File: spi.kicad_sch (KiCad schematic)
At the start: 24 parts

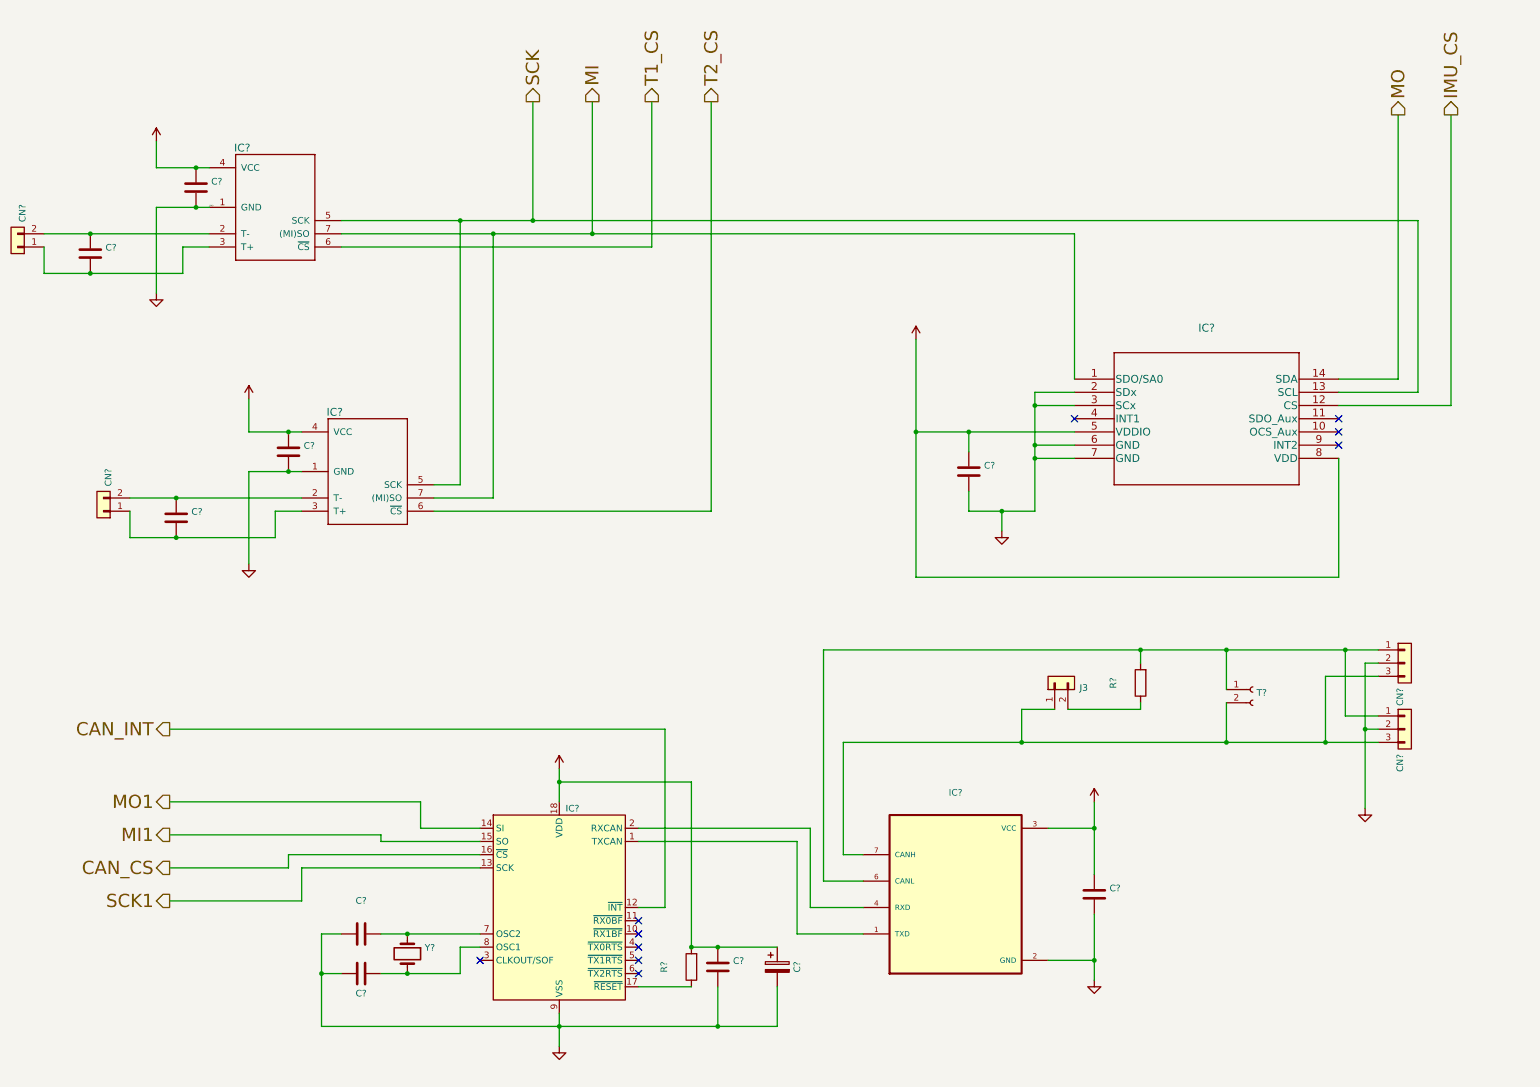
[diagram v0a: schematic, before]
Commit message: fixed power flag in schematic causing error
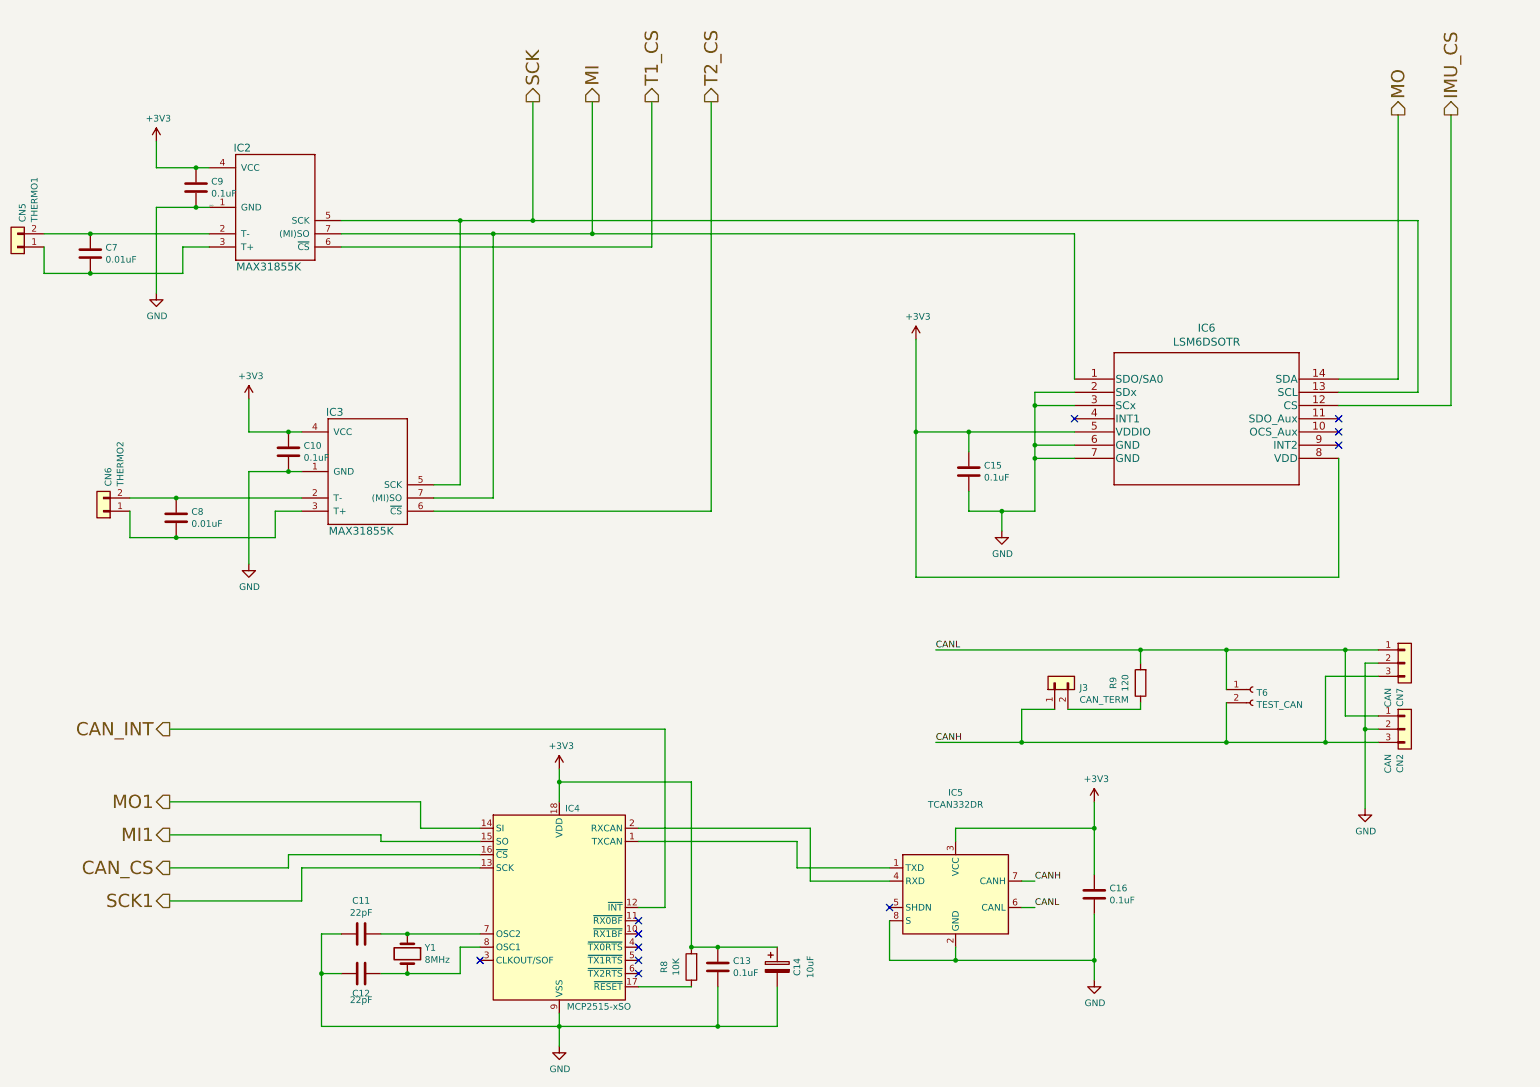
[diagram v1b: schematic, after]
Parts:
- C10, C13, C15, C16, C9: renamed from C?; value (none) -> 0.1uF; footprint (none) -> Capacitor_SMD:C_0805_2012Metric
- C11, C12: renamed from C?; value (none) -> 22pF; footprint (none) -> Capacitor_SMD:C_0805_2012Metric
- C14: renamed from C?; value (none) -> 10uF; footprint (none) -> Capacitor_SMD:C_1206_3216Metric
- C7, C8: renamed from C?; value (none) -> 0.01uF; footprint (none) -> Capacitor_SMD:C_0805_2012Metric
- CN2, CN7: renamed from CN?; value (none) -> CAN; footprint (none) -> telemetry-pcb:molex-sl-1x03-horizontal
- CN5: renamed from CN?; value (none) -> THERMO1; footprint (none) -> telemetry-pcb:ScrewTermPlug1x02
- CN6: renamed from CN?; value (none) -> THERMO2; footprint (none) -> telemetry-pcb:ScrewTermPlug1x02
- IC2, IC3: renamed from IC?; value (none) -> MAX31855K; footprint (none) -> Package_SO:SOIC-8-1EP_3.9x4.9mm_P1.27mm_EP2.29x3mm
- IC4: renamed from IC?; value (none) -> MCP2515-xSO; footprint (none) -> Package_SO:SOIC-18W_7.5x11.6mm_P1.27mm
- IC5: renamed from IC?; value (none) -> TCAN332DR; footprint (none) -> Package_SO:SOIC-8-1EP_3.9x4.9mm_P1.27mm_EP2.29x3mm; symbol telemetry-pcb-rescue:TCAN332DR-TCAN332DR-telemetry-pcb-rescue-telemetry-pcb-rescue -> Interface_CAN_LIN:TCAN330
- IC6: renamed from IC?; value (none) -> LSM6DSOTR; footprint (none) -> telemetry-pcb:LSM6DSOTR
- J3: value (none) -> CAN_TERM; footprint (none) -> Connector_PinHeader_2.54mm:PinHeader_1x02_P2.54mm_Horizontal
- R8: renamed from R?; value (none) -> 10K; footprint (none) -> Resistor_SMD:R_0805_2012Metric
- R9: renamed from R?; value (none) -> 120; footprint (none) -> Resistor_SMD:R_0805_2012Metric
- T6: renamed from T?; value (none) -> TEST_CAN; footprint (none) -> TestPoint:TestPoint_2Pads_Pitch2.54mm_Drill0.8mm
- Y1: renamed from Y?; value (none) -> 8MHz; footprint (none) -> Crystal:Crystal_SMD_HC49-SD
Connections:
- net GND: now also IC5.8 (S)
- net CANL: now reaches CN2.1 (Pin_1), CN7.1 (Pin_1), IC5.6 (CANL), R9.2, T6.1 (Pin_1)
- net CANH: now reaches CN2.3 (Pin_3), CN7.3 (Pin_3), IC5.7 (CANH), J3.1 (Pin_1), T6.2 (Pin_2)
- no-connect marks 10 -> 11

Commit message: hello
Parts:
- removed CN2, CN7: CAN, telemetry-pcb:molex-sl-1x03-horizontal, symbol Connector_Generic:Conn_01x03
- added J4: CAN2, Library:CONN_5569-04A_MOL, symbol 2025-11-01_18-29-52:39301040
- added J5: CAN1, Library:CONN_5569-04A_MOL, symbol 2025-11-01_18-29-52:39301040
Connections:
- net CANH: now also J4.2, J5.2
- net CANL: now also J4.1, J5.1
- net GND: now also J4.3, J4.4, J5.3, J5.4

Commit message: backup
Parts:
- removed J4: CAN2, Library:CONN_5569-04A_MOL, symbol 2025-11-01_18-29-52:39301040
- removed J5: CAN1, Library:CONN_5569-04A_MOL, symbol 2025-11-01_18-29-52:39301040
- added CAN1, CAN2: Conn_01x03, Library:CONN_SD-43650-001_03_MOL, symbol Connector_Generic:Conn_01x03
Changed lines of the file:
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@@
 	)
 	(junction
-		(at 270.51 144.78)
-		(diameter 0)
-		(color 0 0 0 0)
-	)
-	(junction
 		(at 243.84 118.11)
 		(diameter 0)
@@
 	)
 	(junction
-		(at 270.51 125.73)
-		(diameter 0)
-		(color 0 0 0 0)
-	)
-	(junction
 		(at 45.72 36.83)
 		(diameter 0)
@@
 	(wire
 		(pts
-			(xy 270.51 125.73) (xy 274.32 125.73)
-		)
-		(stroke
-			(width 0)
-			(type default)
-		)
-	)
-	(wire
-		(pts
 			(xy 280.67 72.39) (xy 265.43 72.39)
 		)
@@
 	(wire
 		(pts
-			(xy 270.51 144.78) (xy 274.32 144.78)
-		)
-		(stroke
-			(width 0)
-			(type default)
-		)
-	)
-	(wire
-		(pts
 			(xy 184.15 80.01) (xy 184.15 107.95)
 		)
@@
 	(wire
 		(pts
-			(xy 270.51 123.19) (xy 270.51 125.73)
+			(xy 270.51 123.19) (xy 270.51 142.24)
 		)
 		(stroke
@@
 	(wire
 		(pts
-			(xy 270.51 125.73) (xy 270.51 142.24)
-		)
-		(stroke
-			(width 0)
-			(type default)
-		)
-	)
-	(wire
-		(pts
 			(xy 207.01 82.55) (xy 207.01 85.09)
 		)
@@
 	(wire
 		(pts
-			(xy 270.51 144.78) (xy 270.51 153.67)
+			(xy 270.51 142.24) (xy 270.51 153.67)
 		)
 		(stroke
@@
 	(wire
 		(pts
-			(xy 270.51 142.24) (xy 270.51 144.78)
-		)
-		(stroke
-			(width 0)
-			(type default)
-		)
-	)
-	(wire
-		(pts
 			(xy 204.47 166.37) (xy 207.01 166.37)
 		)
@@
 	)
 	(symbol
-		(lib_id "2025-11-01_18-29-52:39301040")
-		(at 287.02 128.27 0)
+		(lib_id "Connector_Generic:Conn_01x03")
+		(at 285.75 138.43 0)
 		(unit 1)
 		(exclude_from_sim no)
@@
 		(on_board yes)
 		(dnp no)
-		(property "Reference" "J5"
-			(at 288.29 120.6499 0)
+		(fields_autoplaced yes)
+		(property "Reference" "CAN2"
+			(at 288.29 137.1599 0)
 			(effects
 				(font
-					(size 1.524 1.524)
+					(size 1.27 1.27)
 				)
 				(justify left)
 			)
 		)
-		(property "Value" "CAN1"
-			(at 279.146 114.3 0)
+		(property "Value" "Conn_01x03"
+			(at 288.29 139.6999 0)
 			(effects
 				(font
-					(size 1.524 1.524)
+					(size 1.27 1.27)
 				)
 				(justify left)
 			)
 		)
-		(property "Footprint" "Library:CONN_5569-04A_MOL"
-			(at 285.242 129.794 0)
+		(property "Footprint" "Library:CONN_SD-43650-001_03_MOL"
+			(at 285.75 138.43 0)
 			(effects
 				(font
 					(size 1.27 1.27)
-					(italic yes)
 				)
+				(hide yes)
 			)
 		)
-		(property "Datasheet" "https://www.molex.com/en-us/products/part-detail-pdf/39301040?display=pdf"
-			(at 274.32 118.11 0)
+		(property "Datasheet" "~"
+			(at 285.75 138.43 0)
 			(effects
 				(font
 					(size 1.27 1.27)
-					(italic yes)
 				)
 				(hide yes)
 			)
 		)
-		(property "Description" ""
-			(at 287.02 128.27 0)
+		(property "Description" "Generic connector, single row, 01x03, script generated (kicad-library-utils/schlib/autogen/connector/)"
+			(at 285.75 138.43 0)
 			(effects
 				(font
@@
 		(pin "1"
 		)
-		(pin "2"
-		)
 		(pin "3"
 		)
-		(pin "4"
+		(pin "2"
 		)
 		(instances
 			(project "telemetry-pcb"
 				(path "/871fe08d-2afd-493a-a8ef-c8aa2cbbb7b9/00000000-0000-0000-0000-00006195e29d"
-					(reference "J5")
+					(reference "CAN2")
 					(unit 1)
 				)
@@
 	)
 	(symbol
-		(lib_id "2025-11-01_18-29-52:39301040")
-		(at 287.02 147.32 0)
+		(lib_id "Connector_Generic:Conn_01x03")
+		(at 284.48 121.92 0)
 		(unit 1)
 		(exclude_from_sim no)
@@
 		(on_board yes)
 		(dnp no)
-		(property "Reference" "J4"
-			(at 288.29 139.6999 0)
+		(fields_autoplaced yes)
+		(property "Reference" "CAN1"
+			(at 287.02 120.6499 0)
 			(effects
 				(font
-					(size 1.524 1.524)
+					(size 1.27 1.27)
 				)
 				(justify left)
 			)
 		)
-		(property "Value" "CAN2"
-			(at 279.4 133.35 0)
+		(property "Value" "Conn_01x03"
+			(at 287.02 123.1899 0)
 			(effects
 				(font
-					(size 1.524 1.524)
+					(size 1.27 1.27)
 				)
 				(justify left)
 			)
 		)
-		(property "Footprint" "Library:CONN_5569-04A_MOL"
-			(at 285.75 148.59 0)
+		(property "Footprint" "Library:CONN_SD-43650-001_03_MOL"
+			(at 284.48 121.92 0)
 			(effects
 				(font
 					(size 1.27 1.27)
-					(italic yes)
 				)
+				(hide yes)
 			)
 		)
-		(property "Datasheet" "https://www.molex.com/en-us/products/part-detail-pdf/39301040?display=pdf"
-			(at 274.32 137.16 0)
+		(property "Datasheet" "~"
+			(at 284.48 121.92 0)
 			(effects
 				(font
 					(size 1.27 1.27)
-					(italic yes)
 				)
 				(hide yes)
 			)
 		)
-		(property "Description" ""
-			(at 287.02 147.32 0)
+		(property "Description" "Generic connector, single row, 01x03, script generated (kicad-library-utils/schlib/autogen/connector/)"
+			(at 284.48 121.92 0)
 			(effects
 				(font
@@
 		(pin "1"
 		)
-		(pin "2"
-		)
 		(pin "3"
 		)
-		(pin "4"
+		(pin "2"
 		)
 		(instances
 			(project ""
 				(path "/871fe08d-2afd-493a-a8ef-c8aa2cbbb7b9/00000000-0000-0000-0000-00006195e29d"
-					(reference "J4")
+					(reference "CAN1")
 					(unit 1)
 				)

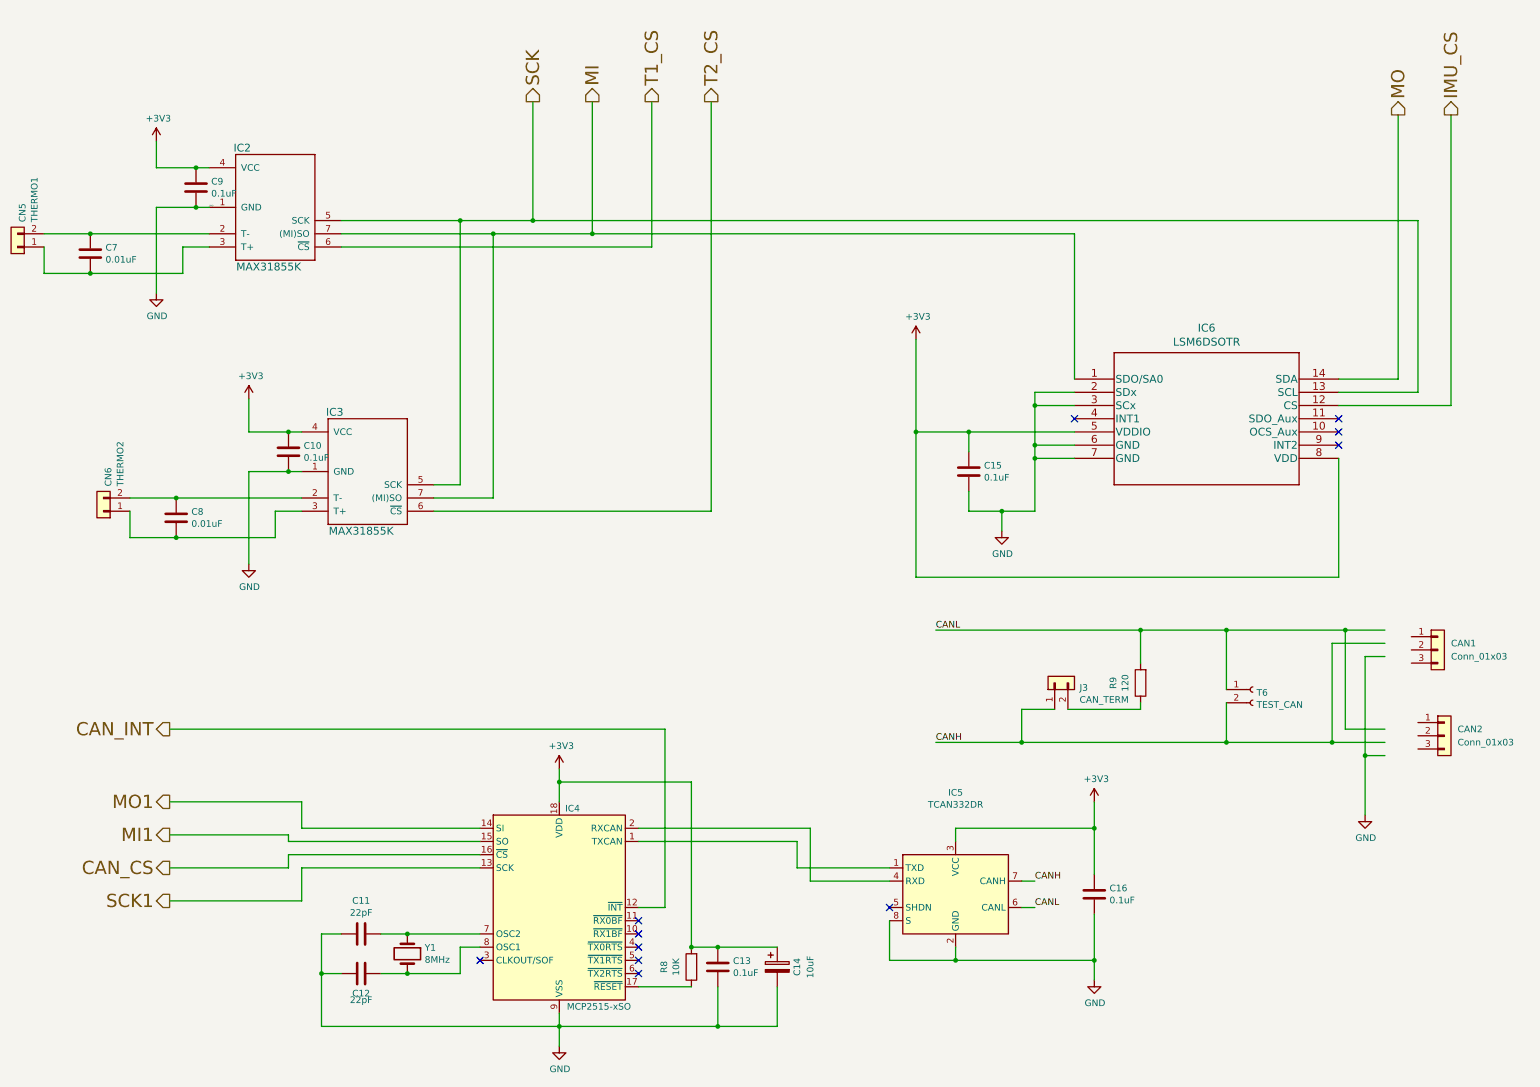
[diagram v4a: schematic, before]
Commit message: Completed PCB routing
new footprints added to Footprints folder, added I2C peripherals page.
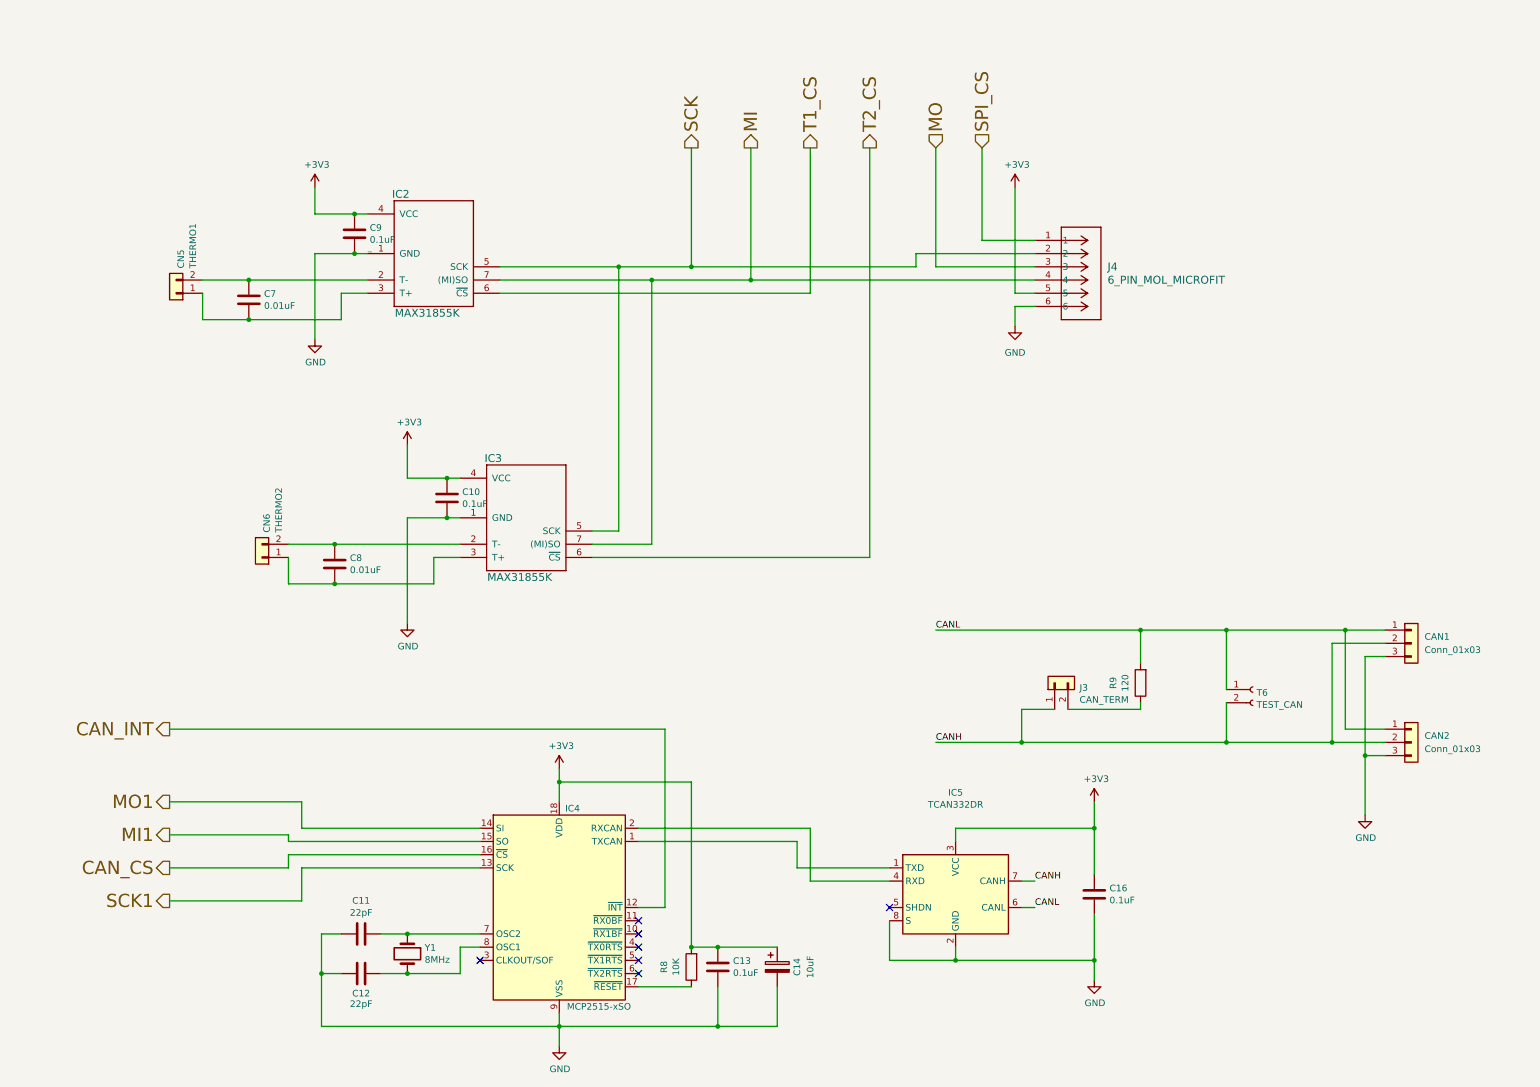
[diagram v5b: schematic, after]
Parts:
- removed C15: 0.1uF, Capacitor_SMD:C_0805_2012Metric, symbol Device:C
- removed IC6: LSM6DSOTR, telemetry-pcb:LSM6DSOTR, symbol telemetry-pcb-rescue:LSM6DSOTR-2021-11-02_20-37-28-telemetry-pcb-rescue-telemet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
- added J4: 6_PIN_MOL_MICROFIT, CONN_SD-43045-001_06_MOL, symbol telemetry_3.0_sch_library:6_PIN_MOL_MICROFIT
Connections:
- net +3V3: now also J4.5
- net CANH: now also CAN1.2 (Pin_2), CAN2.2 (Pin_2)
- net CANL: now also CAN1.1 (Pin_1), CAN2.1 (Pin_1)
- net GND: now also CAN1.3 (Pin_3), CAN2.3 (Pin_3), J4.6
- net MI: now also J4.4
- net MO: now also J4.3
- net SCK: now also J4.2
- new net SPI_CS: J4.1
- no-connect marks 11 -> 7
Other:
- moved on the sheet: C10, C7, C8, C9, CAN1, CAN2, CN5, CN6, IC2, IC3
